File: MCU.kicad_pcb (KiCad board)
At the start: 4 copper layers, 110.3 x 131 mm, 94 parts, among them J1 HSEC8-150-01-X-RA-X, J10 Conn_02x10_Odd_Even, J11 Conn_01x10, J12 Conn_01x10, J13 Conn_01x10, J14 Conn_01x10, J15 Conn_01x02, J16 Conn_02x10_Odd_Even, J17 Conn_02x30_Counter_Clockwise, J18 Conn_01x10, J19 Conn_01x10, J2 Barrel_Jack_MountingPin, J20 Conn_01x02, J21 Conn_02x10_Odd_Even, J22 Conn_01x02, J23 Conn_01x02, J32 Conn_01x02, J4 Conn_02x30_Counter_Clockwise, J5 Conn_02x10_Odd_Even, J6 Conn_01x02, J7 Conn_01x10, J8 Conn_01x10, J9 Conn_01x02, U1 TPS76333, U11 TPS76333, U12 TXB0104RUT, U14 TPS76333, U2 TXB0104RUT, U3 LMR36510ADDA, U6 TXB0104RUT, U8 TPS76333, U9 TXB0104RUT

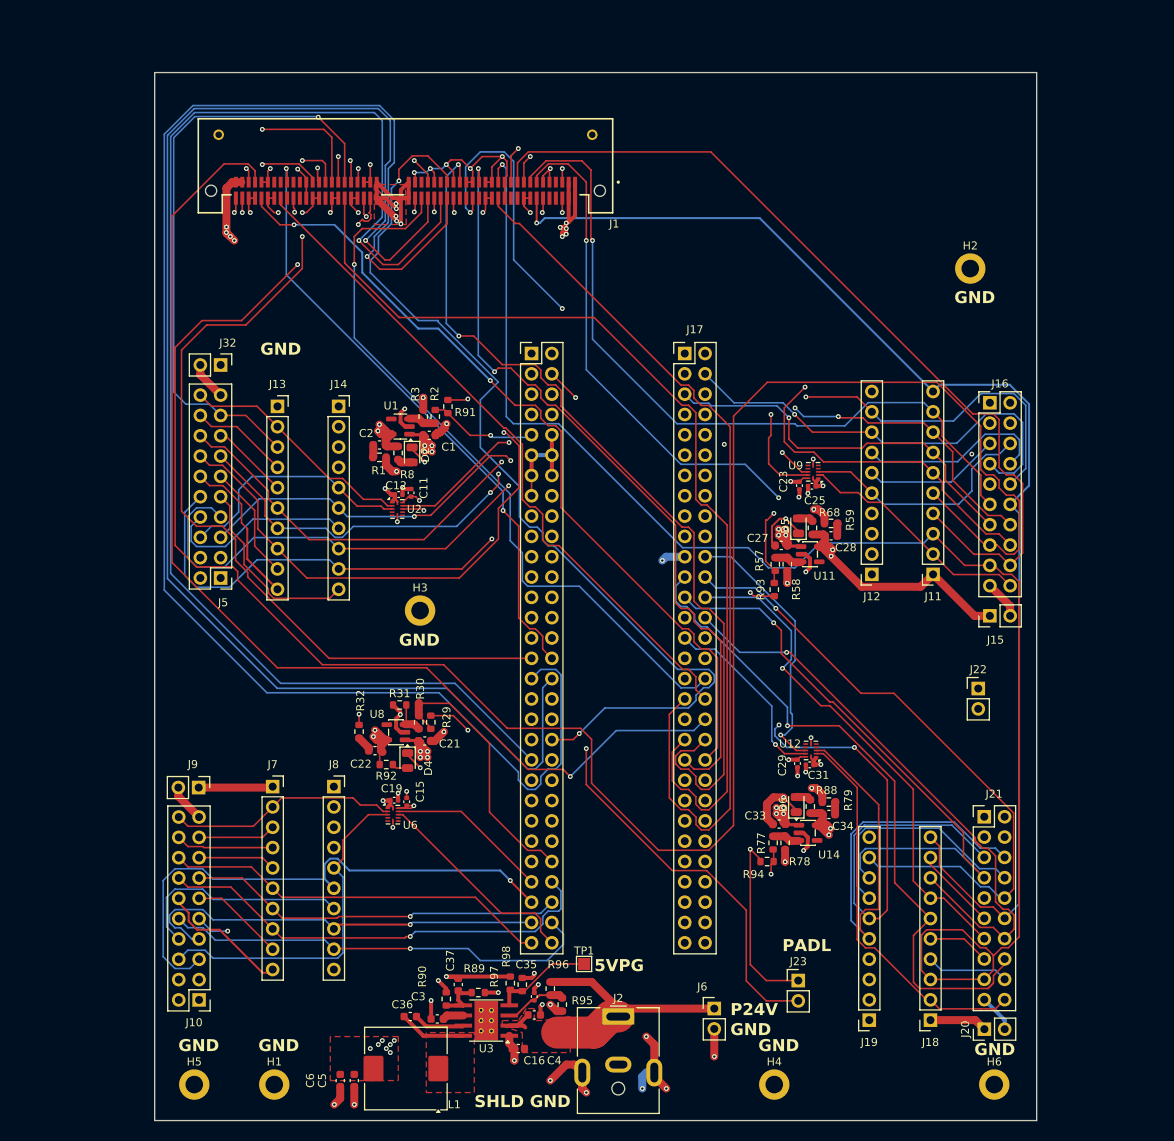
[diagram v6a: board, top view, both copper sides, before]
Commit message: OPCL via LevelShifters
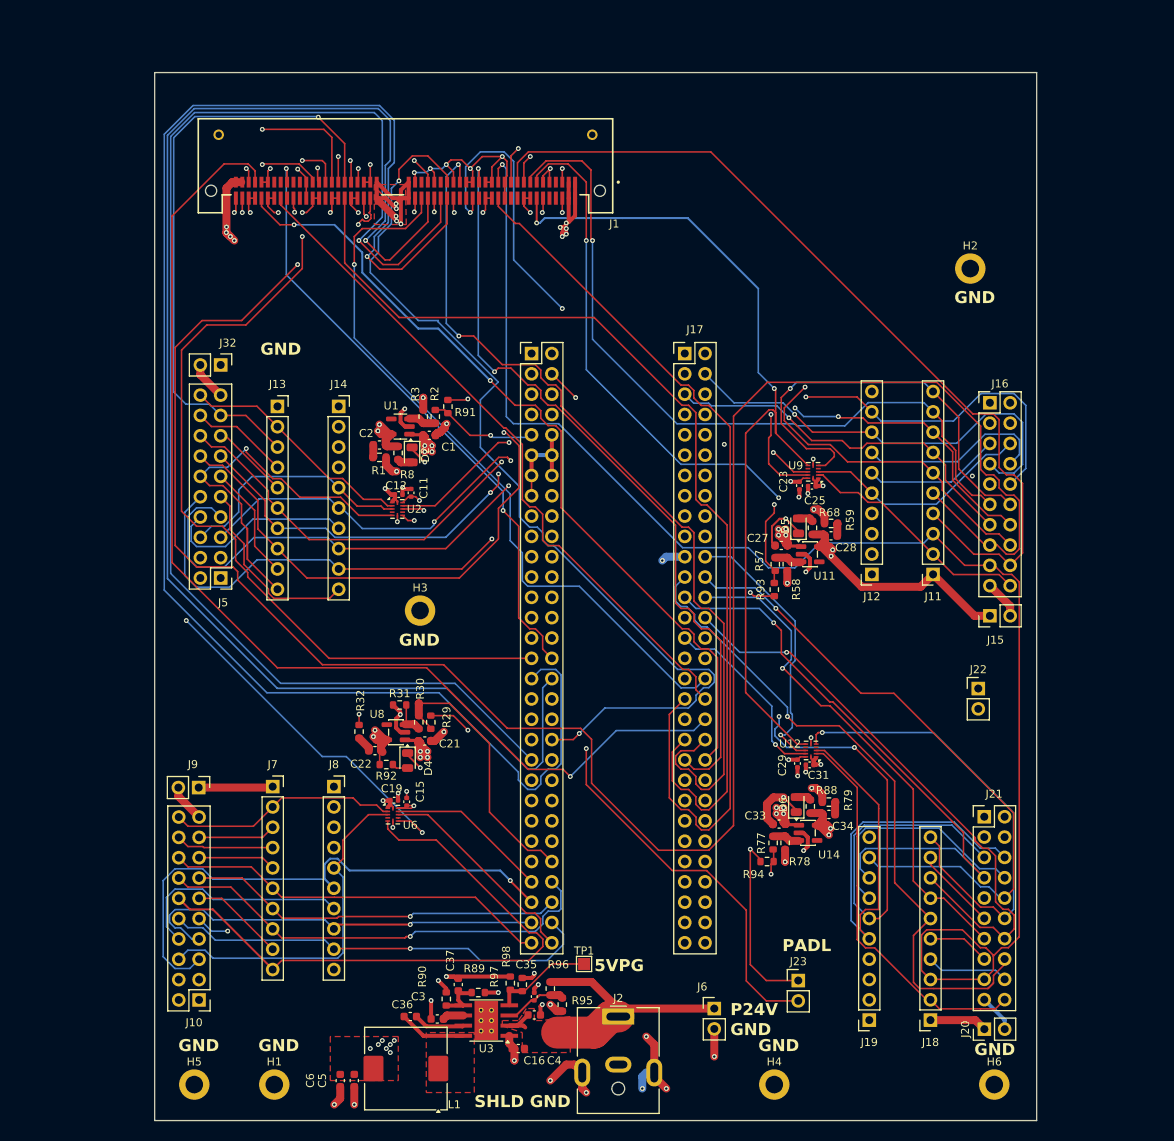
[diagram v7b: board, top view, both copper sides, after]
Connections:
- J10 pad 12: OPCL_US -> /GP_SUB1/P15_TRIP_OC
- J11 pad 10: OPCL_DS -> /GP_SUB2/P15_TRIP_OC
- J13 pad 10: OPCL_US -> /GP_SUB/P15_TRIP_OC
- J16 pad 12: OPCL_DS -> /GP_SUB2/P15_TRIP_OC
- J18 pad 10: OPCL_DS -> /GP_SUB3/P15_TRIP_OC
- J21 pad 12: OPCL_DS -> /GP_SUB3/P15_TRIP_OC
- J5 pad 12: OPCL_US -> /GP_SUB/P15_TRIP_OC
- J7 pad 10: OPCL_US -> /GP_SUB1/P15_TRIP_OC
- U12 pad 5: unconnected-(U12-A4-Pad5) -> /GP_SUB3/P15_TRIP_OC
- U12 pad 7: unconnected-(U12-B4-Pad7) -> OPCL_DS
- U2 pad 5: unconnected-(U2-A4-Pad5) -> /GP_SUB/P15_TRIP_OC
- U2 pad 7: unconnected-(U2-B4-Pad7) -> OPCL_US
- U6 pad 5: unconnected-(U6-A4-Pad5) -> /GP_SUB1/P15_TRIP_OC
- U6 pad 7: unconnected-(U6-B4-Pad7) -> OPCL_US
- U9 pad 5: unconnected-(U9-A4-Pad5) -> /GP_SUB2/P15_TRIP_OC
- U9 pad 7: unconnected-(U9-B4-Pad7) -> OPCL_DS
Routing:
- net OPCL_US: track 269.6 -> 172.4 mm, vias 1 -> 4
- net /GP_SUB1/P15_TRIP_OC: track 0.00 -> 77.8 mm
- net /GP_SUB3/P15_TRIP_OC: track 0.00 -> 58.7 mm, vias 0 -> 1
- net /GP_SUB2/P15_TRIP_OC: track 0.00 -> 53.8 mm, vias 0 -> 1
- net /GP_SUB/P15_TRIP_OC: track 0.00 -> 48.2 mm, vias 0 -> 1
- net OPCL_DS: track 156.6 -> 109.7 mm, vias 1 -> 2
- net A0V: track 252.6 -> 250.5 mm
- net /GP_SUB/P12_GP_OPCL_T2: track 53.6 -> 55.4 mm
- net /GP_SUB2/P16_FET_OCF: track 30.4 -> 28.8 mm
- net /GP_SUB2/P11_EN_PSD: track 48.1 -> 46.5 mm
- net /GP_SUB2/P7_VIMOSA1: track 56.3 -> 54.8 mm
- net /GP_SUB3/P7_VIMOSA1: track 85.0 -> 84.3 mm
- net /GP_SUB2/TP16_Pin16: track 27.9 -> 28.5 mm
- net DS_NCS_C1: track 94.0 -> 94.7 mm
